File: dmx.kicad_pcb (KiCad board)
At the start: 4 copper layers, 66 x 18 mm, 40 parts, among them J102 CORTEX-DEBUG, J103 JAE_DX07S016JA3, J201 SJ2-25504B-SMT-TR, SW101 SW_Push, SW102 SW_Push, U101 TPS78433QWDRBRQ1, U102 ATSAMD51G, U201 LTC2863, Y101 32k768

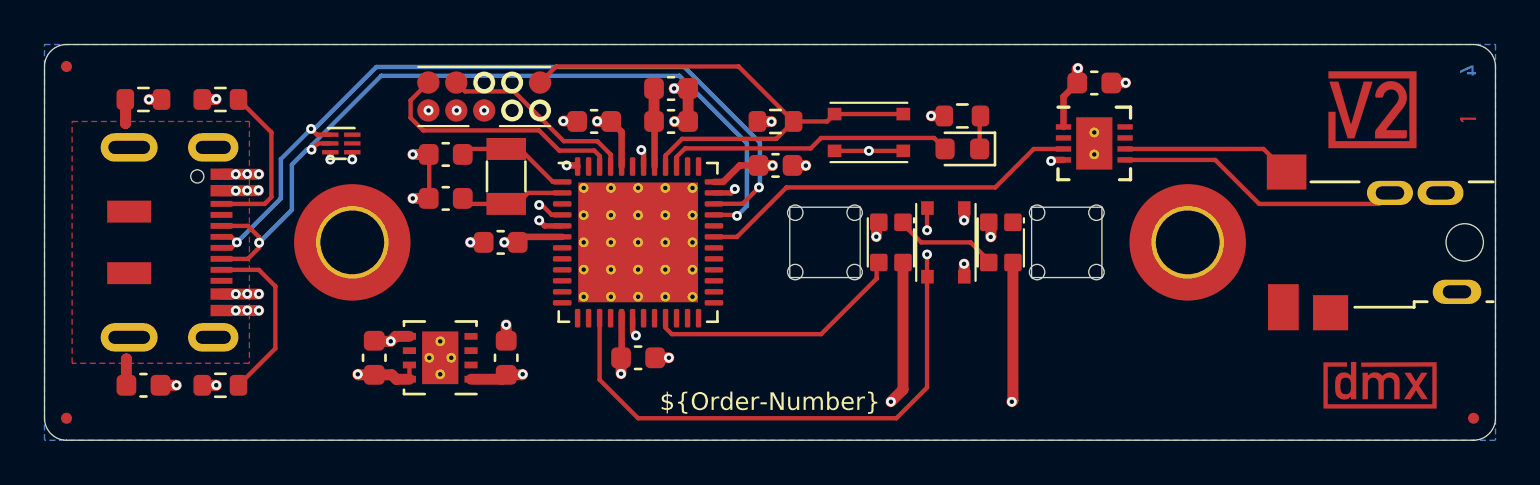
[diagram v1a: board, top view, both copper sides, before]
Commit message: Update TRS socket
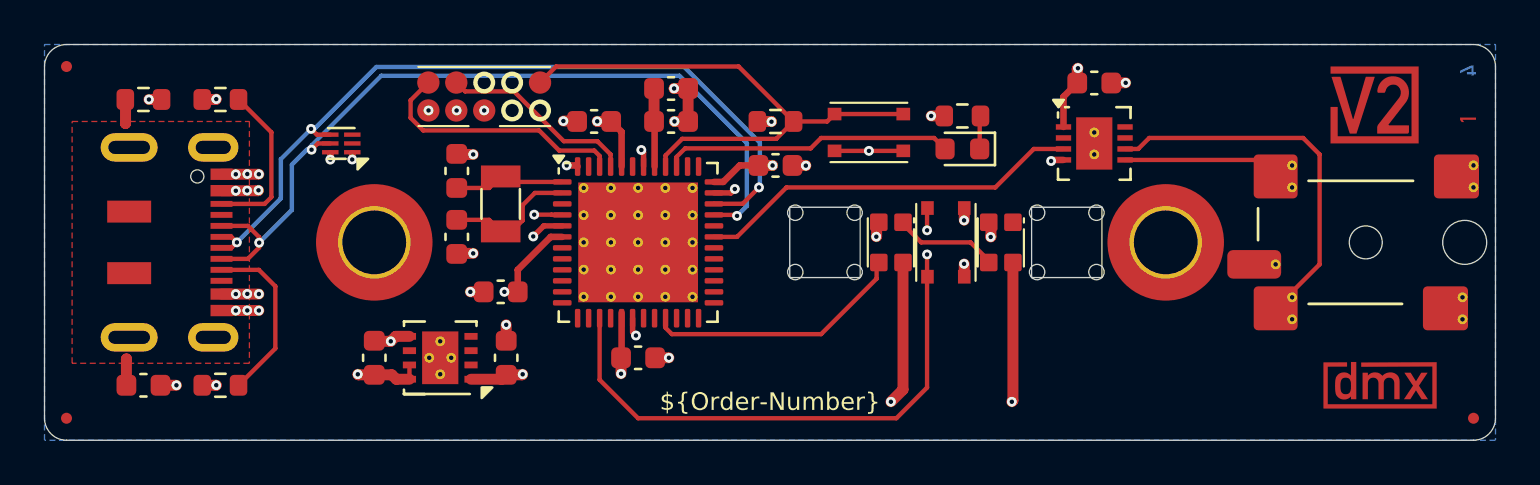
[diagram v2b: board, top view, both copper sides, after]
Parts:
- J201: value SJ2-25504B-SMT-TR -> SJ2-25404B-SMT-TR; footprint V2_Connector_Audio:CUI_SJ2-25504B-SMT-TR -> V2_Connector_Audio:CUI_SJ2-25404B-SMT-TR
- U101: value TPS78433QWDRBRQ1 -> TPS78433QWDRBRQ1
- moved C109 2.25 mm to (137.8, 108.2)
- moved C102 1.82 mm to (135.8, 105.8), turned to -90 degrees
- moved Y101 1.27 mm to (137.8, 104.2)
- moved SPACER101 1.00 mm to (132.0, 106.0)
- moved SPACER102 1.00 mm to (168.0, 106.0)
- moved C101 0.90 mm to (135.8, 102.8), turned to 90 degrees
- moved ICON102 0.25 mm to (177.5, 99.8)
- moved J201 0.25 mm to (177.5, 106.0)
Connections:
- net Net-(J201-R1) renamed /DMX Out/Ring
- J201 pad 2: unconnected-(J201-T-Pad2) -> /DMX Out/Tip
- U201 pad 6: Net-(U201-Z) -> /DMX Out/Tip
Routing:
- net /DMX Out/Tip: track 0.00 -> 17.2 mm
- net Net-(U201-Z): track 7.78 -> 0.00 mm
- net /DMX Out/Ring: track 13.1 -> 7.16 mm
- net GND: track 29.2 -> 27.6 mm
- net /XOUT32: track 4.81 -> 6.15 mm
- net +3V3: track 18.7 -> 19.6 mm
